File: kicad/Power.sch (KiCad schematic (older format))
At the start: 18 parts

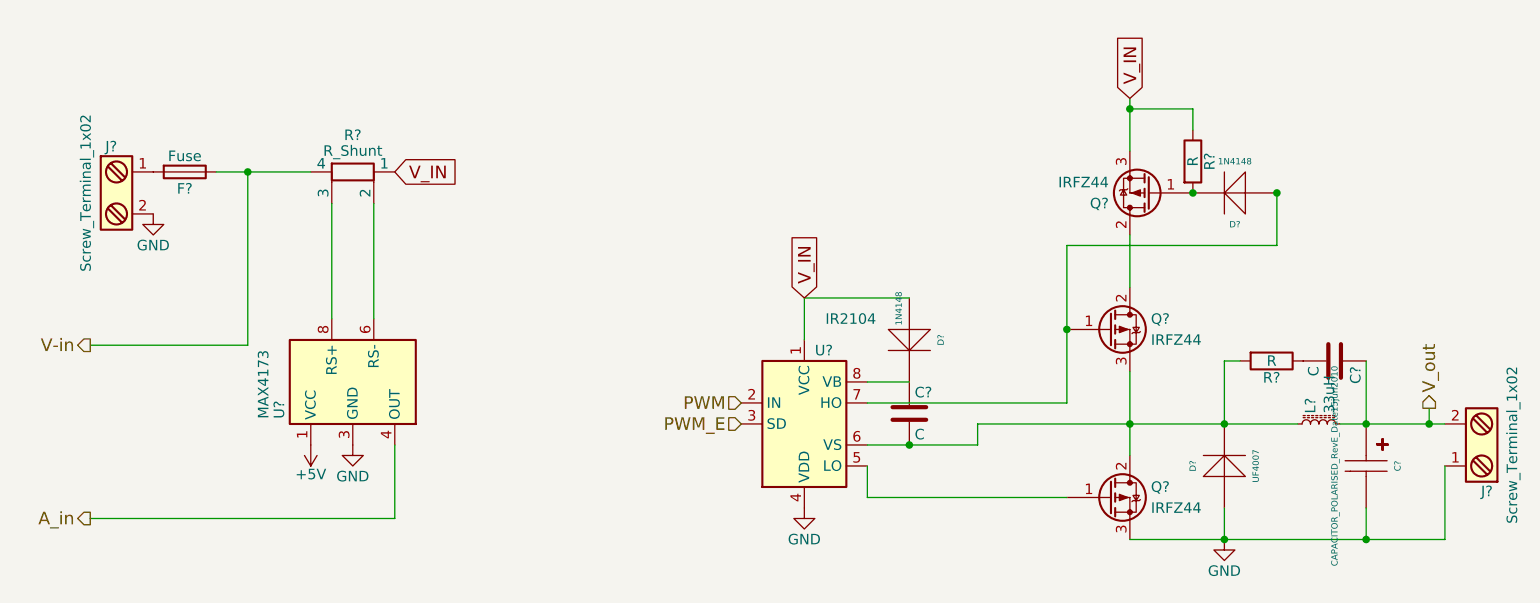
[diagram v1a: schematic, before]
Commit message: Build hierarchy schematic
From the first schematic split in two page uController and Power
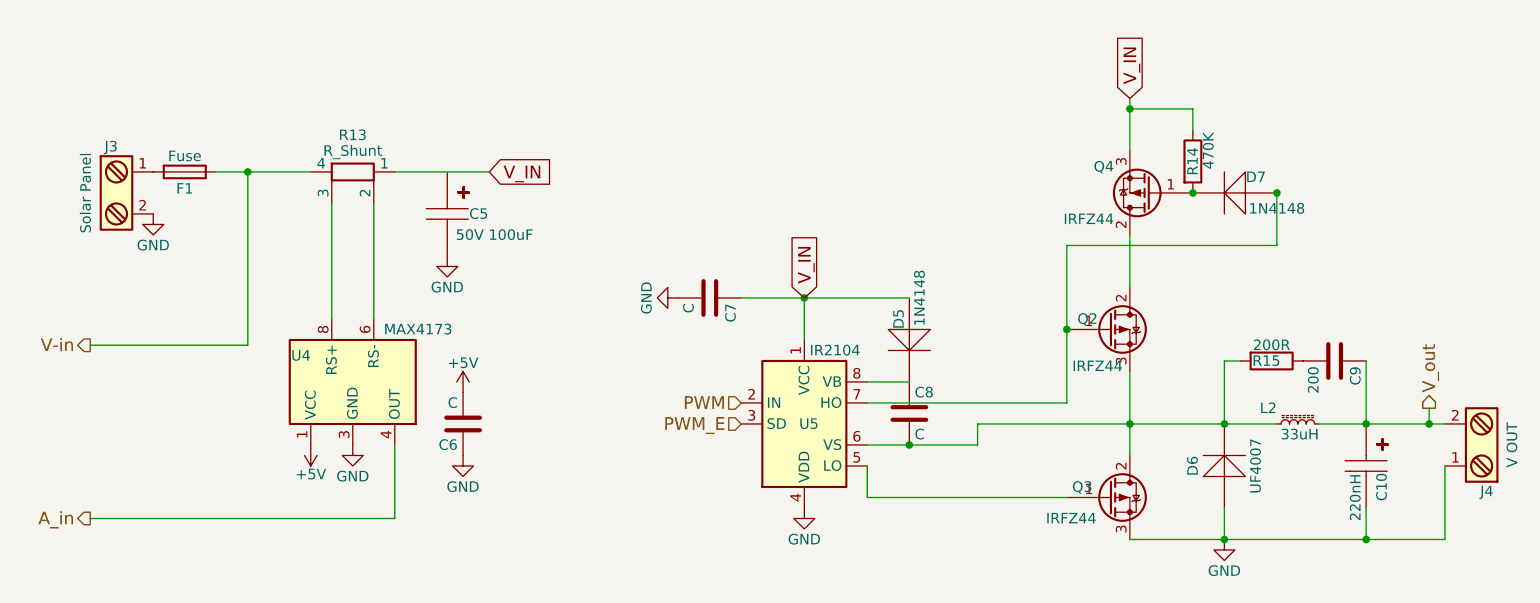
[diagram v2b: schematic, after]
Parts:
- added C5: 50V 100uF, symbol CAPACITOR_POLARISED_RevE_Date15jun2010
- added C6, C7: C, symbol C
- C10: renamed from C?; value CAPACITOR_POLARISED_RevE_Date15jun2010 -> 220nH
- C9: renamed from C?; value C -> 200
- J3: renamed from J?; value Screw_Terminal_1x02 -> Solar Panel
- J4: renamed from J?; value Screw_Terminal_1x02 -> V OUT
- R14: renamed from R?; value R -> 470K
- R15: renamed from R?; value R -> 200R
- gave numbers to parts that had none: 12
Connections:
- net +5V: now also C6.2
- net GND: now also C5.2, C6.1, C7.2
- net V_IN: now also C7.1
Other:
- moved on the sheet: L2
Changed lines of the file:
@@
 $EndDescr
 $Comp
-L Screw_Terminal_1x02 J?
-U 1 1 5B803474
-P 1650 2150
-F 0 "J?" H 1650 2400 50  0000 C TNN
-F 1 "Screw_Terminal_1x02" V 1500 2150 50  0000 C TNN
-F 2 "" H 1650 1925 50  0001 C CNN
-F 3 "" H 1625 2150 50  0001 C CNN
-	1    1650 2150
-	1    0    0    -1
-$EndComp
-$Comp
-L Fuse F?
+L Fuse F1
 U 1 1 5B80361D
 P 2000 2050
-F 0 "F?" V 2080 2050 50  0000 C CNN
+F 0 "F1" V 2080 2050 50  0000 C CNN
 F 1 "Fuse" V 1925 2050 50  0000 C CNN
 F 2 "" V 1930 2050 50  0001 C CNN
@@
 $EndComp
 $Comp
-L GND #PWR?
+L GND #PWR31
 U 1 1 5B803654
 P 1850 2250
-F 0 "#PWR?" H 1850 2000 50  0001 C CNN
+F 0 "#PWR31" H 1850 2000 50  0001 C CNN
 F 1 "GND" H 1850 2100 50  0000 C CNN
 F 2 "" H 1850 2250 50  0001 C CNN
@@
 	1    0    0    -1
 $EndComp
-Text GLabel 3000 2050 2    60   Input ~ 0
+Text GLabel 3450 2050 2    60   Input ~ 0
 V_IN
 $Comp
-L Q_PMOS_GDS Q?
+L Q_PMOS_GDS Q4
 U 1 1 5B8037D3
 P 6600 2150
-F 0 "Q?" H 6800 2200 50  0000 L CNN
-F 1 "IRFZ44" H 6800 2100 50  0000 L CNN
+F 0 "Q4" H 6775 2025 50  0000 L CNN
+F 1 "IRFZ44" H 6775 2275 50  0000 L CNN
 F 2 "" H 6800 2250 50  0001 C CNN
 F 3 "" H 6600 2150 50  0001 C CNN
@@
 $EndComp
 $Comp
-L Q_PMOS_GDS Q?
+L Q_PMOS_GDS Q2
 U 1 1 5B80383F
 P 6400 2800
-F 0 "Q?" H 6600 2850 50  0000 L CNN
-F 1 "IRFZ44" H 6600 2750 50  0000 L CNN
+F 0 "Q2" H 6250 2850 50  0000 L CNN
+F 1 "IRFZ44" H 6225 2625 50  0000 L CNN
 F 2 "" H 6600 2900 50  0001 C CNN
 F 3 "" H 6400 2800 50  0001 C CNN
@@
 $EndComp
 $Comp
-L Q_PMOS_GDS Q?
+L Q_PMOS_GDS Q3
 U 1 1 5B803873
 P 6400 3600
-F 0 "Q?" H 6600 3650 50  0000 L CNN
-F 1 "IRFZ44" H 6600 3550 50  0000 L CNN
+F 0 "Q3" H 6225 3650 50  0000 L CNN
+F 1 "IRFZ44" H 6100 3500 50  0000 L CNN
 F 2 "" H 6600 3700 50  0001 C CNN
 F 3 "" H 6400 3600 50  0001 C CNN
@@
 $EndComp
 $Comp
-L IR2104 U?
+L IR2104 U5
 U 1 1 5B8060D0
 P 4950 3250
-F 0 "U?" H 5000 3600 50  0000 L CNN
-F 1 "IR2104" H 5050 3750 50  0000 L CNN
+F 0 "U5" H 4925 3250 50  0000 L CNN
+F 1 "IR2104" H 4975 3600 50  0000 L CNN
 F 2 "SOIC-8" H 5150 2900 50  0001 C CIN
 F 3 "" H 4950 3250 50  0001 C CNN
@@
 $EndComp
 $Comp
-L DIODE-STANDARD_RevE_Date15jun2010 D?
+L DIODE-STANDARD_RevE_Date15jun2010 D7
 U 1 1 5B80643B
 P 7000 2150
-F 0 "D?" H 7000 2300 30  0000 C CNN
-F 1 "1N4148" H 7000 2000 30  0000 C CNN
+F 0 "D7" H 6900 2075 50  0000 C CNN
+F 1 "1N4148" H 6800 2225 50  0000 C CNN
 F 2 "" H 7000 2150 60  0001 C CNN
 F 3 "" H 7000 2150 60  0001 C CNN
@@
 V_IN
 $Comp
-L L_Core_Ferrite_Small L?
+L L_Core_Ferrite_Small L2
 U 1 1 5B8067DC
-P 7400 3250
-F 0 "L?" H 7450 3290 50  0000 L CNN
-F 1 "33uH" H 7450 3200 50  0000 L CNN
-F 2 "" H 7400 3250 50  0001 C CNN
-F 3 "" H 7400 3250 50  0001 C CNN
-	1    7400 3250
+P 7300 3250
+F 0 "L2" V 7375 3350 50  0000 L CNN
+F 1 "33uH" V 7250 3150 50  0000 L CNN
+F 2 "" H 7300 3250 50  0001 C CNN
+F 3 "" H 7300 3250 50  0001 C CNN
+	1    7300 3250
 	0    -1   -1   0
 $EndComp
@@
 	6500 3000 6500 3400
 Wire Wire Line
-	5775 3250 7300 3250
+	5775 3250 7200 3250
 Connection ~ 6500 3250
 Text GLabel 4950 2650 1    60   Input ~ 0
 V_IN
 $Comp
-L DIODE-STANDARD_RevE_Date15jun2010 D?
+L DIODE-STANDARD_RevE_Date15jun2010 D5
 U 1 1 5B806DC1
 P 5450 2850
-F 0 "D?" H 5450 3000 30  0000 C CNN
-F 1 "1N4148" H 5300 2800 30  0000 C CNN
+F 0 "D5" H 5350 2800 50  0000 C CNN
+F 1 "1N4148" H 5250 2900 50  0000 C CNN
 F 2 "" H 5450 2850 60  0001 C CNN
 F 3 "" H 5450 2850 60  0001 C CNN
@@
 	5250 3050 5450 3050
 Wire Wire Line
-	5450 2650 4950 2650
+	4650 2650 5450 2650
 Wire Wire Line
 	4950 2650 4950 2850
 $Comp
-L C C?
+L C C8
 U 1 1 5B806F78
 P 5450 3200
-F 0 "C?" H 5475 3300 50  0000 L CNN
+F 0 "C8" H 5475 3300 50  0000 L CNN
 F 1 "C" H 5475 3100 50  0000 L CNN
 F 2 "" H 5488 3050 50  0001 C CNN
@@
 Wire Wire Line
 	5250 3350 5775 3350
-$Comp
-L R_Shunt R?
-U 1 1 5B82012D
-P 2800 2050
-F 0 "R?" V 2625 2050 50  0000 C CNN
-F 1 "R_Shunt" V 2700 2050 50  0000 C CNN
-F 2 "" V 2730 2050 50  0001 C CNN
-F 3 "" H 2800 2050 50  0001 C CNN
-	1    2800 2050
-	0    1    1    0
-$EndComp
 Wire Wire Line
 	2150 2050 2600 2050
 $Comp
-L MAX4173 U?
+L MAX4173 U4
 U 1 1 5B820270
 P 2800 3050
-F 0 "U?" H 2625 3400 50  0000 L CNN
-F 1 "MAX4173" H 2625 3475 50  0000 L CNN
+F 0 "U4" V 2925 3250 50  0000 L CNN
+F 1 "MAX4173" V 3050 2575 50  0000 L CNN
 F 2 "SOIC-8" H 2800 2700 50  0001 C CIN
 F 3 "" H 2800 3050 50  0001 C CNN
@@
 A_in
 $Comp
-L +5V #PWR?
+L +5V #PWR32
 U 1 1 5B82066B
 P 2600 3350
-F 0 "#PWR?" H 2600 3200 50  0001 C CNN
+F 0 "#PWR32" H 2600 3200 50  0001 C CNN
 F 1 "+5V" H 2600 3490 50  0000 C CNN
 F 2 "" H 2600 3350 50  0001 C CNN
@@
 $EndComp
 $Comp
-L GND #PWR?
+L GND #PWR33
 U 1 1 5B8206A3
 P 2800 3350
-F 0 "#PWR?" H 2800 3100 50  0001 C CNN
+F 0 "#PWR33" H 2800 3100 50  0001 C CNN
 F 1 "GND" H 2800 3200 50  0000 C CNN
 F 2 "" H 2800 3350 50  0001 C CNN
@@
 Connection ~ 6200 2800
 $Comp
-L R R?
+L R R14
 U 1 1 5B83631E
 P 6800 2000
-F 0 "R?" V 6880 2000 50  0000 C CNN
-F 1 "R" V 6800 2000 50  0000 C CNN
+F 0 "R14" V 6800 2000 50  0000 C CNN
+F 1 "470K" V 6875 2050 50  0000 C CNN
 F 2 "" V 6730 2000 50  0001 C CNN
 F 3 "" H 6800 2000 50  0001 C CNN
@@
 	5250 3600 5250 3450
 $Comp
-L GND #PWR?
+L GND #PWR38
 U 1 1 5B83651E
 P 4950 3650
-F 0 "#PWR?" H 4950 3400 50  0001 C CNN
+F 0 "#PWR38" H 4950 3400 50  0001 C CNN
 F 1 "GND" H 4950 3500 50  0000 C CNN
 F 2 "" H 4950 3650 50  0001 C CNN
@@
 $EndComp
 $Comp
-L GND #PWR?
+L GND #PWR39
 U 1 1 5B83654C
 P 6950 3800
-F 0 "#PWR?" H 6950 3550 50  0001 C CNN
+F 0 "#PWR39" H 6950 3550 50  0001 C CNN
 F 1 "GND" H 6950 3650 50  0000 C CNN
 F 2 "" H 6950 3800 50  0001 C CNN
@@
 $EndComp
 $Comp
-L DIODE-STANDARD_RevE_Date15jun2010 D?
+L DIODE-STANDARD_RevE_Date15jun2010 D6
 U 1 1 5B83657A
 P 6950 3450
-F 0 "D?" H 6950 3600 30  0000 C CNN
-F 1 "UF4007" H 6950 3300 30  0000 C CNN
+F 0 "D6" H 6950 3600 50  0000 C CNN
+F 1 "UF4007" H 6950 3300 50  0000 C CNN
 F 2 "" H 6950 3450 60  0001 C CNN
 F 3 "" H 6950 3450 60  0001 C CNN
@@
 Connection ~ 6950 3250
 $Comp
-L R R?
+L R R15
 U 1 1 5B836C21
 P 7175 2950
-F 0 "R?" V 7255 2950 50  0000 C CNN
-F 1 "R" V 7175 2950 50  0000 C CNN
+F 0 "R15" V 7175 2925 50  0000 C CNN
+F 1 "200R" V 7100 2950 50  0000 C CNN
 F 2 "" V 7105 2950 50  0001 C CNN
 F 3 "" H 7175 2950 50  0001 C CNN
@@
 $EndComp
 $Comp
-L C C?
+L C C9
 U 1 1 5B836C7C
 P 7475 2950
-F 0 "C?" H 7500 3050 50  0000 L CNN
-F 1 "C" H 7500 2850 50  0000 L CNN
+F 0 "C9" H 7500 3050 50  0000 L CNN
+F 1 "200" H 7500 2850 50  0000 L CNN
 F 2 "" H 7513 2800 50  0001 C CNN
 F 3 "" H 7475 2950 50  0001 C CNN
@@
 	6950 2950 6950 3250
 Wire Wire Line
-	7500 3250 8000 3250
+	7400 3250 8000 3250
 Wire Wire Line
 	7625 2950 7625 3250
 Connection ~ 7625 3250
 $Comp
-L CAPACITOR_POLARISED_RevE_Date15jun2010 C?
+L CAPACITOR_POLARISED_RevE_Date15jun2010 C10
 U 1 1 5B836DDB
 P 7625 3450
-F 0 "C?" H 7625 3600 30  0000 C CNN
-F 1 "CAPACITOR_POLARISED_RevE_Date15jun2010" H 7625 3300 30  0000 C CNN
+F 0 "C10" H 7725 3525 50  0000 C CNN
+F 1 "220nH" H 7775 3400 50  0000 C CNN
 F 2 "" H 7625 3450 60  0001 C CNN
 F 3 "" H 7625 3450 60  0001 C CNN
@@
 Connection ~ 7625 3800
 $Comp
-L Screw_Terminal_1x02 J?
+L Screw_Terminal_1x02 J4
 U 1 1 5B836F93
 P 8200 3350
-F 0 "J?" H 8200 3600 50  0000 C TNN
-F 1 "Screw_Terminal_1x02" V 8050 3350 50  0000 C TNN
+F 0 "J4" H 8200 3600 50  0000 C TNN
+F 1 "V OUT" V 8050 3350 50  0000 C TNN
 F 2 "" H 8200 3125 50  0001 C CNN
 F 3 "" H 8175 3350 50  0001 C CNN
@@
 	7925 3175 7925 3250
 Connection ~ 7925 3250
+$Comp
+L C C7
+U 1 1 5B84AD25
+P 4500 2650
+F 0 "C7" H 4525 2750 50  0000 L CNN
+F 1 "C" H 4525 2550 50  0000 L CNN
+F 2 "" H 4538 2500 50  0001 C CNN
+F 3 "" H 4500 2650 50  0001 C CNN
+	1    4500 2650
+	0    1    1    0
+$EndComp
+$Comp
+L GND #PWR37
+U 1 1 5B84AE6F
+P 4350 2650
+F 0 "#PWR37" H 4350 2400 50  0001 C CNN
+F 1 "GND" H 4350 2500 50  0000 C CNN
+F 2 "" H 4350 2650 50  0001 C CNN
+F 3 "" H 4350 2650 50  0001 C CNN
+	1    4350 2650
+	0    1    1    0
+$EndComp
+Connection ~ 4950 2650
+$Comp
+L CAPACITOR_POLARISED_RevE_Date15jun2010 C5
+U 1 1 5B84B2BA
+P 3250 2250
+F 0 "C5" V 3250 2400 50  0000 C CNN
+F 1 "50V 100uF" V 3350 2475 50  0000 C CNN
+F 2 "" H 3250 2250 60  0001 C CNN
+F 3 "" H 3250 2250 60  0001 C CNN
+	1    3250 2250
+	0    1    1    0
+$EndComp
+Wire Wire Line
+	3000 2050 3450 2050
+$Comp
+L GND #PWR34
+U 1 1 5B84B3BD
+P 3250 2450
+F 0 "#PWR34" H 3250 2200 50  0001 C CNN
+F 1 "GND" H 3250 2300 50  0000 C CNN
+F 2 "" H 3250 2450 50  0001 C CNN
+F 3 "" H 3250 2450 50  0001 C CNN
+	1    3250 2450
+	1    0    0    -1
+$EndComp
+$Comp
+L Screw_Terminal_1x02 J3
+U 1 1 5B803474
+P 1650 2150
+F 0 "J3" H 1650 2400 50  0000 C TNN
+F 1 "Solar Panel" V 1500 2150 50  0000 C TNN
+F 2 "" H 1650 1925 50  0001 C CNN
+F 3 "" H 1625 2150 50  0001 C CNN
+	1    1650 2150
+	1    0    0    -1
+$EndComp
+$Comp
+L R_Shunt R13
+U 1 1 5B82012D
+P 2800 2050
+F 0 "R13" V 2625 2050 50  0000 C CNN
+F 1 "R_Shunt" V 2700 2050 50  0000 C CNN
+F 2 "" V 2730 2050 50  0001 C CNN
+F 3 "" H 2800 2050 50  0001 C CNN
+	1    2800 2050
+	0    1    1    0
+$EndComp
+$Comp
+L C C6
+U 1 1 5B8526B2
+P 3325 3250
+F 0 "C6" H 3350 3350 50  0000 L CNN
+F 1 "C" H 3350 3150 50  0000 L CNN
+F 2 "" H 3363 3100 50  0001 C CNN
+F 3 "" H 3325 3250 50  0001 C CNN
+	1    3325 3250
+	-1   0    0    1
+$EndComp
+$Comp
+L GND #PWR36
+U 1 1 5B852751
+P 3325 3400
+F 0 "#PWR36" H 3325 3150 50  0001 C CNN
+F 1 "GND" H 3325 3250 50  0000 C CNN
+F 2 "" H 3325 3400 50  0001 C CNN
+F 3 "" H 3325 3400 50  0001 C CNN
+	1    3325 3400
+	1    0    0    -1
+$EndComp
+$Comp
+L +5V #PWR35
+U 1 1 5B8527E0
+P 3325 3100
+F 0 "#PWR35" H 3325 2950 50  0001 C CNN
+F 1 "+5V" H 3325 3240 50  0000 C CNN
+F 2 "" H 3325 3100 50  0001 C CNN
+F 3 "" H 3325 3100 50  0001 C CNN
+	1    3325 3100
+	1    0    0    -1
+$EndComp
 $EndSCHEMATC

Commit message: Update of schematical
Two resistor of 10R on gate mosfet
Just for the test remove the third mosfet before the step-down converter
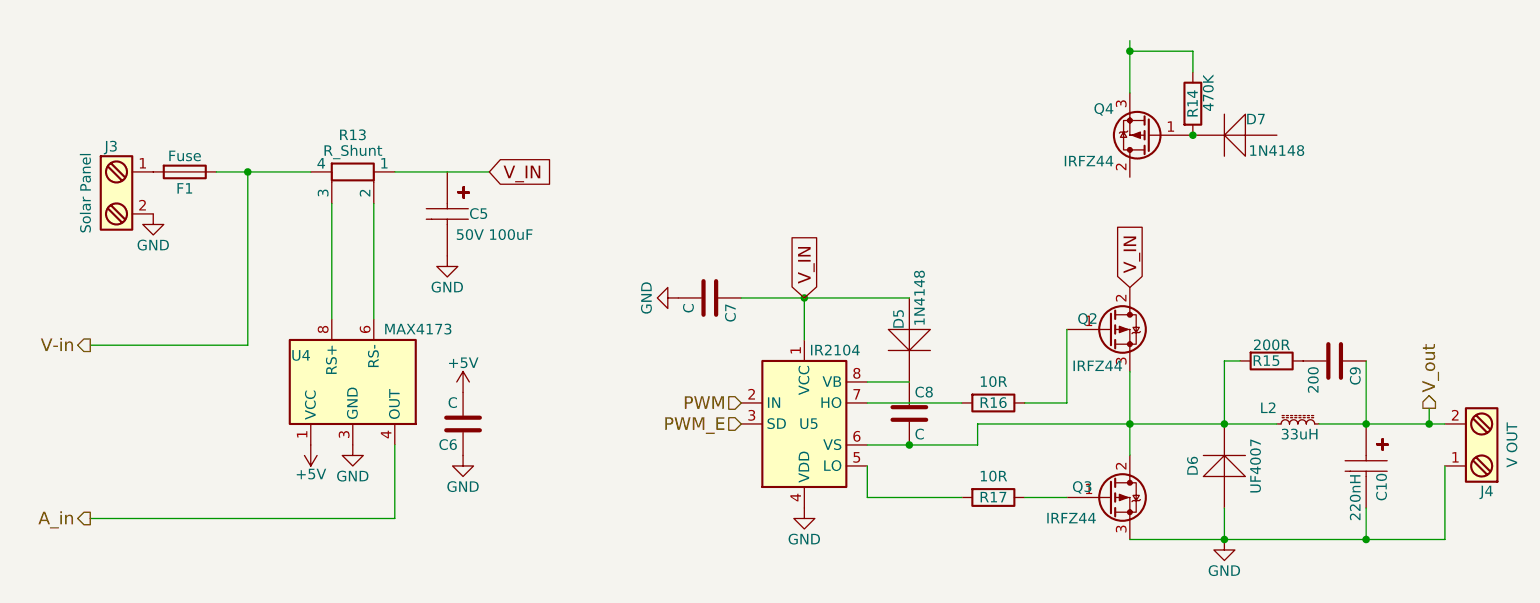
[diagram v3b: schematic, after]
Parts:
- added R16, R17: 10R, symbol R
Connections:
- net V_IN: now also Q2.2 (D); no longer Q4.3 (S), R14.1
- net at Q4.2 (D): no longer Q2.2 (D)
- net at Q3.1 (G): now also R17.1; no longer U5.5 (LO)
- new net: Q4.3 (S), R14.1
- new net: Q2.1 (G), R16.1
- new net: R17.2, U5.5 (LO)
- new net: R16.2, U5.7 (HO)
- now unconnected: D7.1 (A)
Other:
- moved on the sheet: D7, Q4, R14
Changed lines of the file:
@@
 LIBS:valves
 LIBS:Altera
-LIBS:Msystem
 LIBS:motor_drivers
-LIBS:79xx-Regler-BuildingBlock_ModB_RevA-cache
-LIBS:Switch
-LIBS:Display
-LIBS:Relay
 LIBS:relays
-LIBS:nxp
 LIBS:dc-dc
 LIBS:MPPT-cache
@@
 L Q_PMOS_GDS Q4
 U 1 1 5B8037D3
-P 6600 2150
-F 0 "Q4" H 6775 2025 50  0000 L CNN
-F 1 "IRFZ44" H 6775 2275 50  0000 L CNN
-F 2 "" H 6800 2250 50  0001 C CNN
-F 3 "" H 6600 2150 50  0001 C CNN
-	1    6600 2150
+P 6600 1875
+F 0 "Q4" H 6775 1750 50  0000 L CNN
+F 1 "IRFZ44" H 6775 2000 50  0000 L CNN
+F 2 "" H 6800 1975 50  0001 C CNN
+F 3 "" H 6600 1875 50  0001 C CNN
+	1    6600 1875
 	-1   0    0    1
 $EndComp
@@
 L DIODE-STANDARD_RevE_Date15jun2010 D7
 U 1 1 5B80643B
-P 7000 2150
-F 0 "D7" H 6900 2075 50  0000 C CNN
-F 1 "1N4148" H 6800 2225 50  0000 C CNN
-F 2 "" H 7000 2150 60  0001 C CNN
-F 3 "" H 7000 2150 60  0001 C CNN
-	1    7000 2150
+P 7000 1875
+F 0 "D7" H 6900 1800 50  0000 C CNN
+F 1 "1N4148" H 6800 1950 50  0000 C CNN
+F 2 "" H 7000 1875 60  0001 C CNN
+F 3 "" H 7000 1875 60  0001 C CNN
+	1    7000 1875
 	-1   0    0    1
 $EndComp
-Text GLabel 6500 1700 1    60   Input ~ 0
+Text GLabel 6500 2600 1    60   Input ~ 0
 V_IN
 $Comp
@@
 $EndComp
 Wire Wire Line
-	6500 1700 6500 1950
-Wire Wire Line
-	6500 2600 6500 2350
+	6500 1425 6500 1675
 Wire Wire Line
 	6500 3000 6500 3400
@@
 	5775 3350 5775 3250
 Connection ~ 5450 3350
-Wire Wire Line
-	6200 3150 5250 3150
-Wire Wire Line
-	6200 2400 6200 3150
-Wire Wire Line
-	6200 2400 7200 2400
-Wire Wire Line
-	7200 2400 7200 2150
-Connection ~ 6200 2800
 $Comp
 L R R14
 U 1 1 5B83631E
-P 6800 2000
-F 0 "R14" V 6800 2000 50  0000 C CNN
-F 1 "470K" V 6875 2050 50  0000 C CNN
-F 2 "" V 6730 2000 50  0001 C CNN
-F 3 "" H 6800 2000 50  0001 C CNN
-	1    6800 2000
-	1    0    0    -1
-$EndComp
-Connection ~ 6800 2150
-Connection ~ 7200 2150
-Wire Wire Line
-	6800 1850 6800 1750
-Wire Wire Line
-	6800 1750 6500 1750
-Connection ~ 6500 1750
-Wire Wire Line
-	6200 3600 5250 3600
+P 6800 1725
+F 0 "R14" V 6800 1725 50  0000 C CNN
+F 1 "470K" V 6875 1775 50  0000 C CNN
+F 2 "" V 6730 1725 50  0001 C CNN
+F 3 "" H 6800 1725 50  0001 C CNN
+	1    6800 1725
+	1    0    0    -1
+$EndComp
+Connection ~ 6800 1875
+Wire Wire Line
+	6800 1575 6800 1475
+Wire Wire Line
+	6800 1475 6500 1475
+Connection ~ 6500 1475
 Wire Wire Line
 	5250 3600 5250 3450
@@
 	1    0    0    -1
 $EndComp
+$Comp
+L R R16
+U 1 1 5EABF4D0
+P 5850 3150
+F 0 "R16" V 5850 3150 50  0000 C CNN
+F 1 "10R" V 5750 3150 50  0000 C CNN
+F 2 "" V 5780 3150 50  0000 C CNN
+F 3 "" H 5850 3150 50  0000 C CNN
+	1    5850 3150
+	0    1    1    0
+$EndComp
+$Comp
+L R R17
+U 1 1 5EABF559
+P 5850 3600
+F 0 "R17" V 5850 3600 50  0000 C CNN
+F 1 "10R" V 5750 3600 50  0000 C CNN
+F 2 "" V 5780 3600 50  0000 C CNN
+F 3 "" H 5850 3600 50  0000 C CNN
+	1    5850 3600
+	0    1    1    0
+$EndComp
+Wire Wire Line
+	6000 3600 6200 3600
+Wire Wire Line
+	5700 3600 5250 3600
+Wire Wire Line
+	6200 3150 6000 3150
+Wire Wire Line
+	5700 3150 5250 3150
+Wire Wire Line
+	6200 2800 6200 3150
 $EndSCHEMATC
